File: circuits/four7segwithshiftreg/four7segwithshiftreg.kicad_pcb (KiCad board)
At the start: 2 copper layers, 85.3 x 39.4 mm, 45 parts, among them J1 Conn_01x05, U1 74HC595, U2 74HC595, U3 D198K, U4 D198K, U5 74HC595, U6 74HC595, U7 D198K, U8 D198K

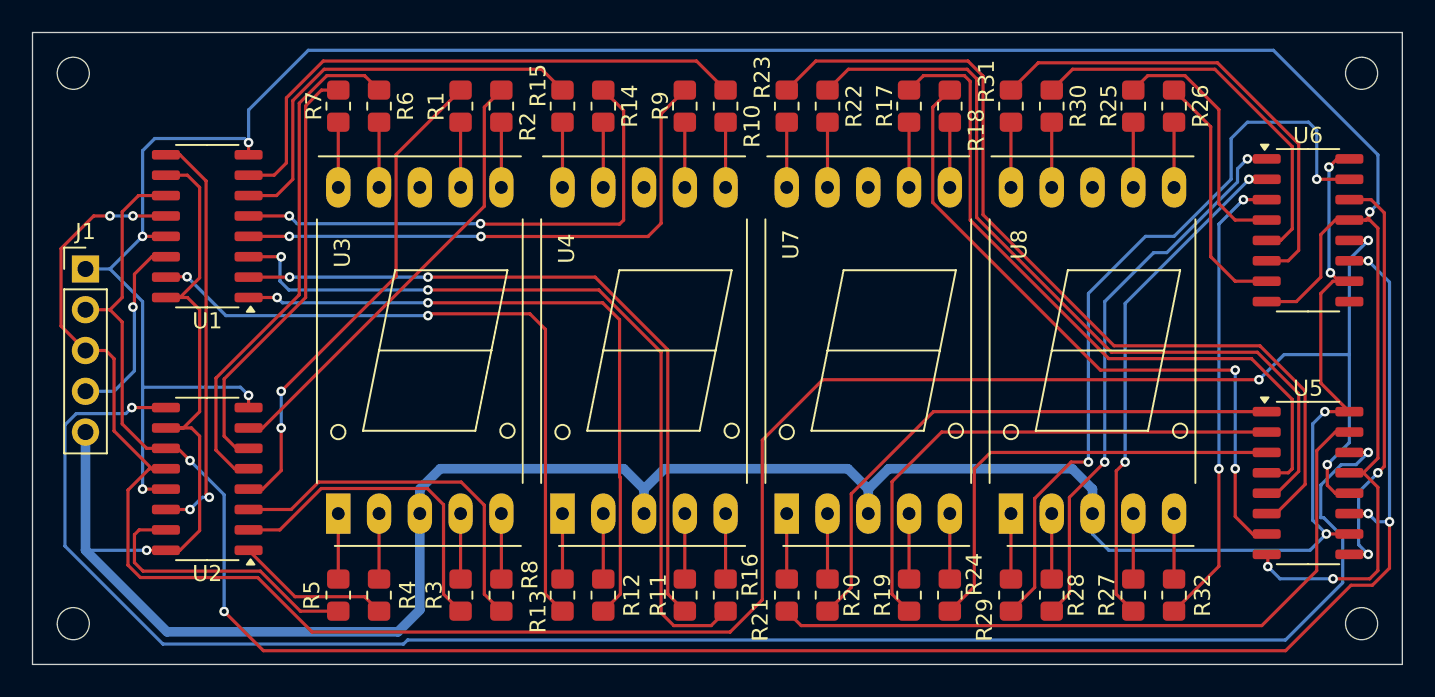
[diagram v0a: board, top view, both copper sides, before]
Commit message: Correct the length of the sparkfun 7-Segment footprint
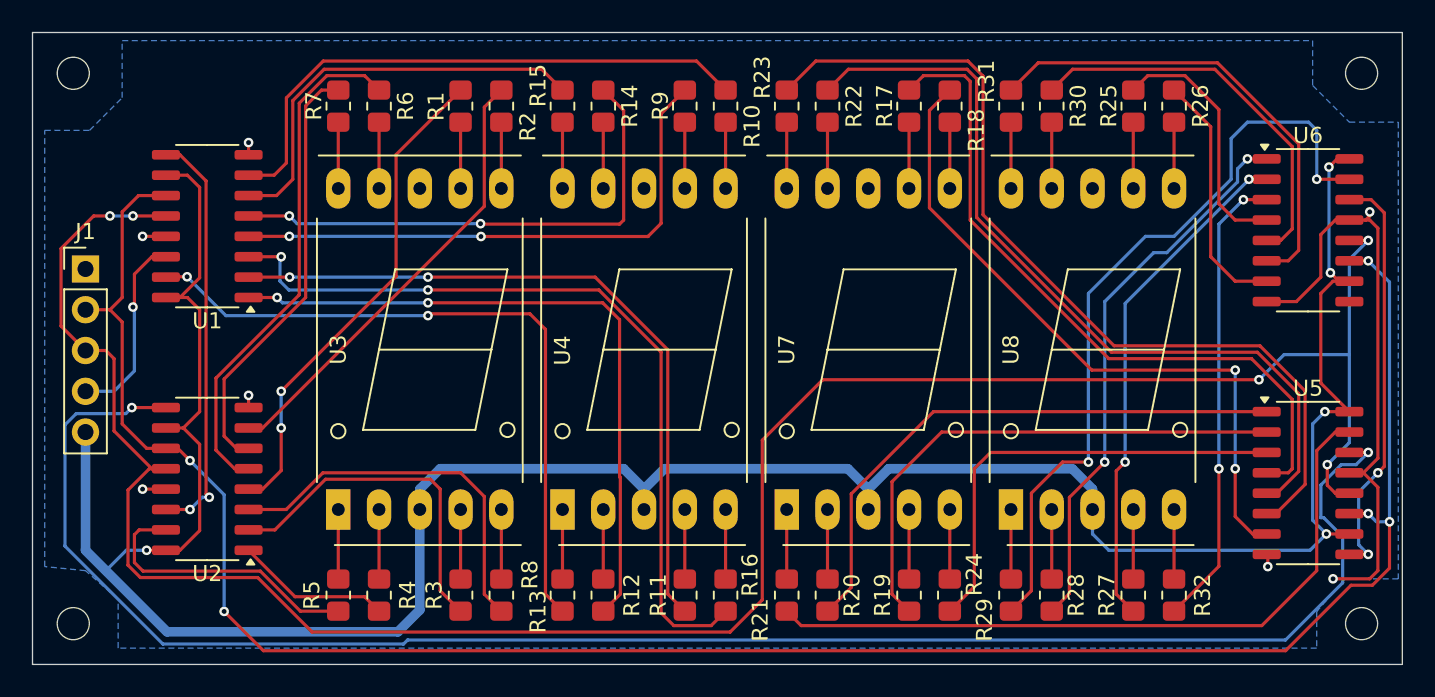
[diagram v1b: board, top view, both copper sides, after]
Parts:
- moved U3 0.05 mm to (127.8, 103.6)
- moved U4 0.05 mm to (141.7, 103.6)
- moved U7 0.05 mm to (155.7, 103.6)
- moved U8 0.05 mm to (169.7, 103.6)
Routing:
- net GND: track 165.5 -> 42.6 mm
- net +5V: track 173.4 -> 170.8 mm
- net Net-(U2-QC): track 20.7 -> 21.6 mm
- net Net-(U2-QD): track 23.0 -> 23.8 mm
- added copper zone on B.Cu, net GND
